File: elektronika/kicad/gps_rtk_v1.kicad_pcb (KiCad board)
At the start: 2 copper layers, 80 x 72 mm, 16 parts, among them J1 GNSS LC29HEA, J2 OLED SSD1306, J3 IMU BNO085 v2, J4 Buck-boost 3V3, J5 TP4056 USB-C, SW1 user, U1 ESP32-WROOM-32

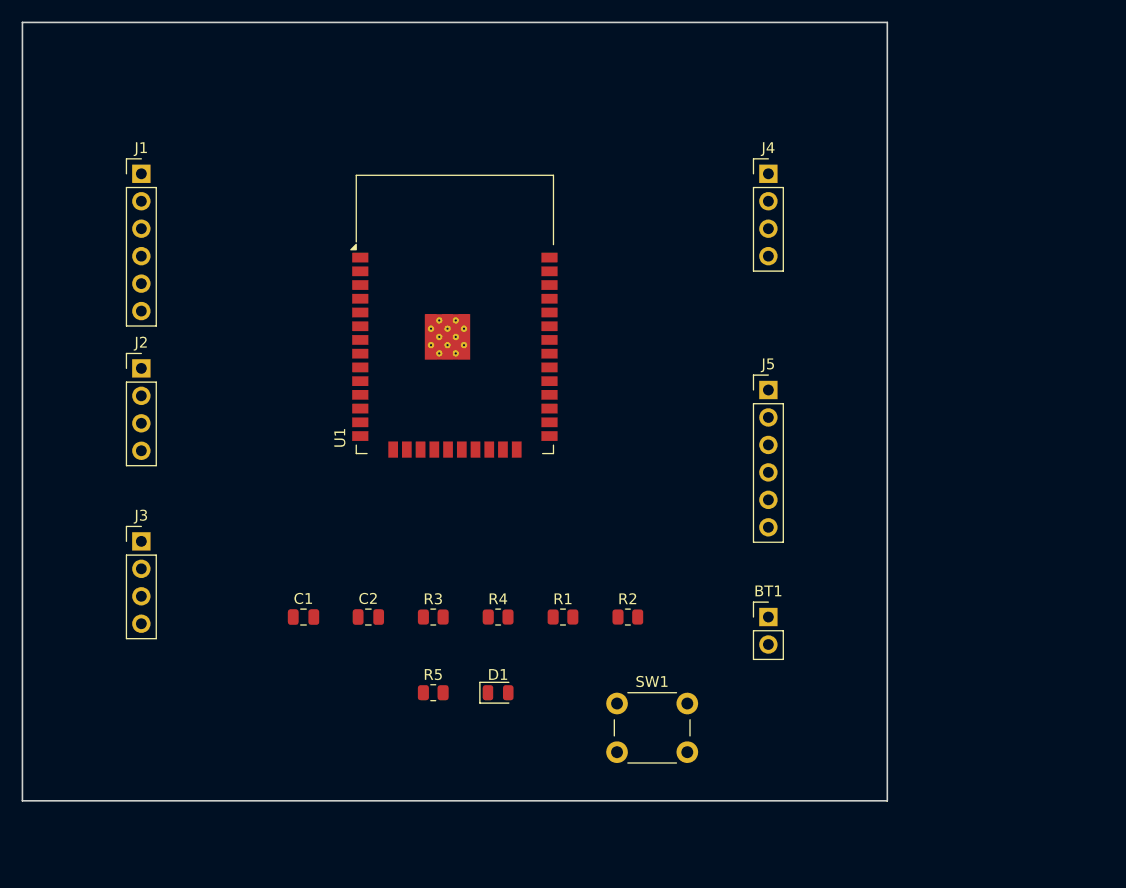
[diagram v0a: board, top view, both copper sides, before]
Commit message: elektronika/kicad: PCB jako carrier - wszystkie moduly w gniazdach
- ESP32 jako devkit (2x PinSocket 1x19, pinout DevKitC V4); EN/5V wolne (auto-reset/LDO devkitu),
  zasilanie na pin 3V3
- moduly GNSS/OLED/IMU/TP4056/buck + ogniwo jako gniazda zenskie PinSocket; pasywy SMD/THT na carrierze
- 17 footprintow, DRC 0 naruszen; 44 pady = trasowanie (ratsnest)
- gen/gen_pcb.py przepisany na carrier; render 3D PNG + 2D SVG odswiezone
- UWAGA: zweryfikuj rozstaw gniazd ESP32 (0.9 in) i pinout pod swoj devkit

Co-Authored-By: Claude Opus 4.8 (1M context) <noreply@anthropic.com>
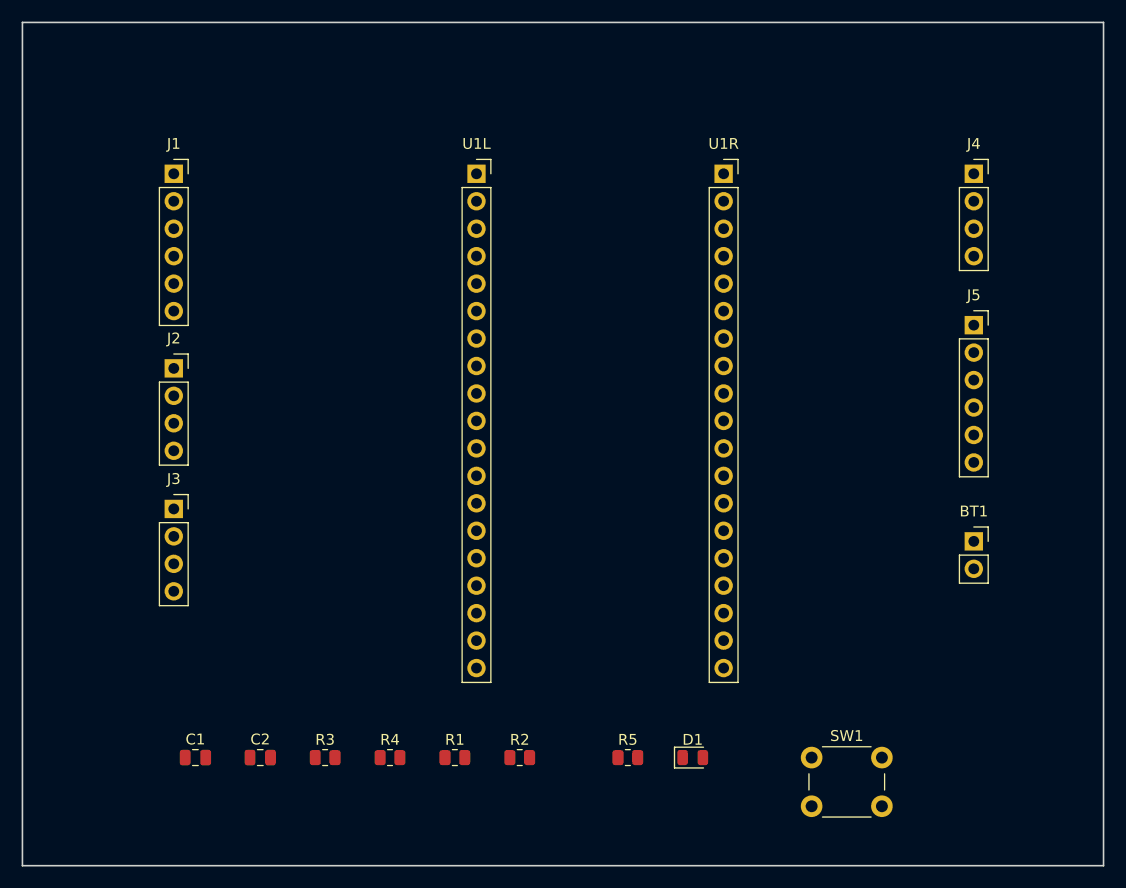
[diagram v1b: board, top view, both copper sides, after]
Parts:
- removed U1: ESP32-WROOM-32, ESP32-WROOM-32
- added U1L: ESP32-DevKitC (lewa), PinSocket_1x19_P2.54mm_Vertical, F.Cu at (42.0, 14.0)
- added U1R: ESP32-DevKitC (prawa), PinSocket_1x19_P2.54mm_Vertical, F.Cu at (64.9, 14.0)
- BT1: value 18650 (off-board) -> 18650 (przewody); footprint PinHeader_1x02_P2.54mm_Vertical -> PinSocket_1x02_P2.54mm_Vertical
- J1: value GNSS LC29HEA -> GNSS LC29HEA (modul); footprint PinHeader_1x06_P2.54mm_Vertical -> PinSocket_1x06_P2.54mm_Vertical
- J2: value OLED SSD1306 -> OLED SSD1306 (modul); footprint PinHeader_1x04_P2.54mm_Vertical -> PinSocket_1x04_P2.54mm_Vertical
- J3: value IMU BNO085 v2 -> IMU BNO085 v2 (modul); footprint PinHeader_1x04_P2.54mm_Vertical -> PinSocket_1x04_P2.54mm_Vertical
- J4: value Buck-boost 3V3 -> Buck-boost 3V3 (modul); footprint PinHeader_1x04_P2.54mm_Vertical -> PinSocket_1x04_P2.54mm_Vertical
- J5: value TP4056 USB-C -> TP4056 USB-C (modul); footprint PinHeader_1x06_P2.54mm_Vertical -> PinSocket_1x06_P2.54mm_Vertical
- moved BT1 20.2 mm to (88.0, 48.0)
- moved J5 19.9 mm to (88.0, 28.0)
- moved J4 19.0 mm to (88.0, 14.0)
- moved D1 19.0 mm to (62.0, 68.0)
- moved R5 19.0 mm to (56.0, 68.0)
- moved SW1 18.7 mm to (73.0, 68.0)
- moved C1 16.4 mm to (16.0, 68.0)
- moved C2 16.4 mm to (22.0, 68.0)
- moved R1 16.4 mm to (40.0, 68.0)
- moved R2 16.4 mm to (46.0, 68.0)
- moved R3 16.4 mm to (28.0, 68.0)
- moved R4 16.4 mm to (34.0, 68.0)
- moved J3 4.24 mm to (14.0, 45.0)
- moved J1 3.00 mm to (14.0, 14.0)
- moved J2 3.00 mm to (14.0, 32.0)
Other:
- board size 80 x 72 mm -> 100 x 78 mm

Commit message: elektronika/kicad: PCB carrier pod ESP32 30-pin (DOIT DevKit V1)
- ESP32 z 2x PinSocket 1x19 -> 2x 1x15 (30-pin DOIT DevKit V1); 25 GPIO + EN/3V3/VIN/2xGND
- EN i VIN wolne (auto-reset/LDO devkitu), 3.3V na pin 3V3
- tabela pinow ESP32 w README do weryfikacji z nadrukiem; ESP_ROW_MM=22.86 (rozstaw do pomiaru)
- DRC 0 naruszen; 43 pady = trasowanie; render 3D + SVG odswiezone

Co-Authored-By: Claude Opus 4.8 (1M context) <noreply@anthropic.com>
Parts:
- removed the U1L at (42.0, 14.0)
- removed the U1R at (64.9, 14.0)
- added U1L: ESP32 DevKit V1 (L), PinSocket_1x15_P2.54mm_Vertical, F.Cu at (42.0, 16.0)
- added U1R: ESP32 DevKit V1 (R), PinSocket_1x15_P2.54mm_Vertical, F.Cu at (64.9, 16.0)
- moved BT1 2.00 mm to (88.0, 50.0)
- moved J1 2.00 mm to (14.0, 16.0)
- moved J2 2.00 mm to (14.0, 34.0)
- moved J3 2.00 mm to (14.0, 47.0)
- moved J4 2.00 mm to (88.0, 16.0)
- moved J5 2.00 mm to (88.0, 30.0)
